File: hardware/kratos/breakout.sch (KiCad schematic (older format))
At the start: 3 parts, among them J4 Power Headers, J5 Power terminals, J6 IO Headers

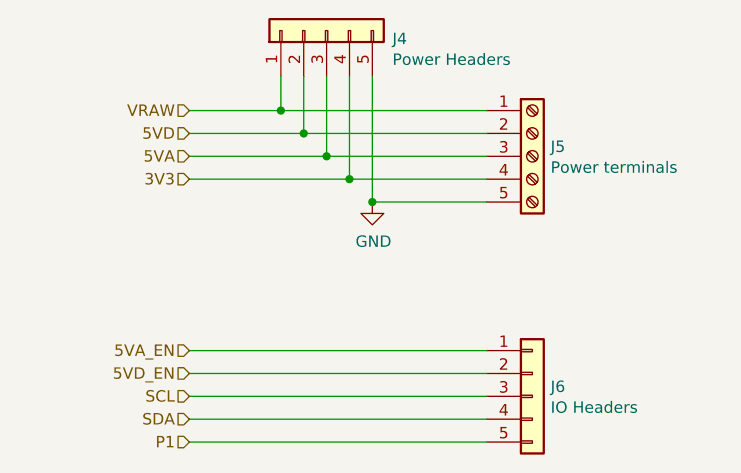
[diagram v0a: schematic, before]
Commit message: Update to linear regulators. Added PCB layout
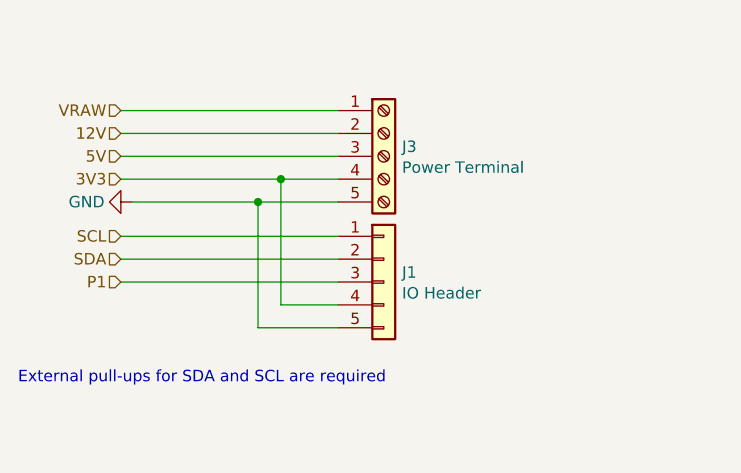
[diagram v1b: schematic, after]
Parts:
- removed J4: Power Headers, Connector_PinSocket_2.54mm:PinSocket_1x05_P2.54mm_Vertical, symbol Connector_Generic:Conn_01x05
- removed J5: Power terminals, TerminalBlock:TerminalBlock_bornier-5_P5.08mm, symbol Connector:Screw_Terminal_01x05
- removed J6: IO Headers, Connector_PinSocket_2.54mm:PinSocket_1x05_P2.54mm_Vertical, symbol Connector_Generic:Conn_01x05
- added J1: IO Header, Connector_PinSocket_2.54mm:PinSocket_1x05_P2.54mm_Vertical, symbol Connector_Generic:Conn_01x05
- added J3: Power Terminal, TerminalBlock:TerminalBlock_bornier-5_P5.08mm, symbol Connector:Screw_Terminal_01x05
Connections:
- net 3V3: now also J1.4 (Pin_4), J3.4 (Pin_4)
- net GND: now also J1.5 (Pin_5), J3.5 (Pin_5)
- net P1: now also J1.3 (Pin_3)
- net SCL: now also J1.1 (Pin_1)
- net SDA: now also J1.2 (Pin_2)
- net VRAW: now also J3.1 (Pin_1)
- new net 12V: J3.2 (Pin_2)
- new net 5V: J3.3 (Pin_3)
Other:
- note added: "External pull-ups for SDA and SCL are required\n"
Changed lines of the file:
@@
 $Descr A4 11693 8268
 encoding utf-8
-Sheet 6 6
+Sheet 3 6
 Title "Power and IO Breakout"
 Date "2021-03-06"
-Rev "REVA"
+Rev "A"
 Comp ""
 Comment1 "Author: Natesh Narain"
@@
 Comment4 ""
 $EndDescr
-Text HLabel 5450 3250 0    50   Input ~ 0
+Text HLabel 5150 3250 0    50   Input ~ 0
 VRAW
-Text HLabel 5450 3350 0    50   Input ~ 0
-5VD
-Text HLabel 5450 3450 0    50   Input ~ 0
-5VA
-Text HLabel 5450 4400 0    50   Input ~ 0
-5VD_EN
-Text HLabel 5450 4300 0    50   Input ~ 0
-5VA_EN
-Text HLabel 5450 3550 0    50   Input ~ 0
+Text HLabel 5150 3450 0    50   Input ~ 0
+5V
+Text HLabel 5150 3550 0    50   Input ~ 0
 3V3
-Text HLabel 5450 4500 0    50   Input ~ 0
+Text HLabel 5150 3800 0    50   Input ~ 0
 SCL
-Text HLabel 5450 4600 0    50   Input ~ 0
+Text HLabel 5150 3900 0    50   Input ~ 0
 SDA
-Text HLabel 5450 4700 0    50   Input ~ 0
+Text HLabel 5150 4000 0    50   Input ~ 0
 P1
 $Comp
-L Connector_Generic:Conn_01x05 J4
-U 1 1 6044FECF
-P 6050 2900
-F 0 "J4" V 6014 2612 50  0000 R CNN
-F 1 "Power Headers" V 5923 2612 50  0000 R CNN
-F 2 "Connector_PinSocket_2.54mm:PinSocket_1x05_P2.54mm_Vertical" H 6050 2900 50  0001 C CNN
-F 3 "~" H 6050 2900 50  0001 C CNN
-	1    6050 2900
-	0    -1   -1   0
+L power:GND #PWR010
+U 1 1 60452371
+P 5200 3650
+F 0 "#PWR010" H 5200 3400 50  0001 C CNN
+F 1 "GND" V 5200 3450 50  0000 C CNN
+F 2 "" H 5200 3650 50  0001 C CNN
+F 3 "" H 5200 3650 50  0001 C CNN
+	1    5200 3650
+	0    1    1    0
 $EndComp
+Text HLabel 5150 3350 0    50   Input ~ 0
+12V
 $Comp
-L Connector:Screw_Terminal_01x05 J5
-U 1 1 60450B14
-P 6950 3450
-F 0 "J5" H 7030 3492 50  0000 L CNN
-F 1 "Power terminals" H 7030 3401 50  0000 L CNN
-F 2 "TerminalBlock:TerminalBlock_bornier-5_P5.08mm" H 6950 3450 50  0001 C CNN
-F 3 "~" H 6950 3450 50  0001 C CNN
-	1    6950 3450
+L Connector:Screw_Terminal_01x05 J3
+U 1 1 604FA9FC
+P 6300 3450
+F 0 "J3" H 6380 3492 50  0000 L CNN
+F 1 "Power Terminal" H 6380 3401 50  0000 L CNN
+F 2 "TerminalBlock:TerminalBlock_bornier-5_P5.08mm" H 6300 3450 50  0001 C CNN
+F 3 "~" H 6300 3450 50  0001 C CNN
+	1    6300 3450
+	1    0    0    -1
+$EndComp
+Text Notes 4700 4450 0    50   ~ 0
+External pull-ups for SDA and SCL are required\n
+Wire Wire Line
+	5150 3250 6100 3250
+Wire Wire Line
+	5150 3350 6100 3350
+Wire Wire Line
+	5150 3450 6100 3450
+Wire Wire Line
+	5200 3650 5750 3650
+$Comp
+L Connector_Generic:Conn_01x05 J1
+U 1 1 60500B75
+P 6300 4000
+F 0 "J1" H 6380 4042 50  0000 L CNN
+F 1 "IO Header" H 6380 3951 50  0000 L CNN
+F 2 "Connector_PinSocket_2.54mm:PinSocket_1x05_P2.54mm_Vertical" H 6300 4000 50  0001 C CNN
+F 3 "~" H 6300 4000 50  0001 C CNN
+	1    6300 4000
 	1    0    0    -1
 $EndComp
 Wire Wire Line
-	5450 3250 5850 3250
+	5150 3800 6100 3800
 Wire Wire Line
-	5450 3350 5950 3350
+	5150 3900 6100 3900
 Wire Wire Line
-	5450 3450 6050 3450
+	5150 4000 6100 4000
 Wire Wire Line
-	5450 3550 6150 3550
-$Comp
-L power:GND #PWR027
-U 1 1 60452371
-P 6250 3650
-F 0 "#PWR027" H 6250 3400 50  0001 C CNN
-F 1 "GND" H 6255 3477 50  0000 C CNN
-F 2 "" H 6250 3650 50  0001 C CNN
-F 3 "" H 6250 3650 50  0001 C CNN
-	1    6250 3650
-	1    0    0    -1
-$EndComp
+	6100 4100 5850 4100
 Wire Wire Line
-	5850 3100 5850 3250
-Connection ~ 5850 3250
+	5850 4100 5850 3550
+Connection ~ 5850 3550
 Wire Wire Line
-	5850 3250 6750 3250
+	5850 3550 6100 3550
 Wire Wire Line
-	5950 3100 5950 3350
-Connection ~ 5950 3350
+	5150 3550 5850 3550
 Wire Wire Line
-	5950 3350 6750 3350
+	6100 4200 5750 4200
 Wire Wire Line
-	6050 3100 6050 3450
-Connection ~ 6050 3450
+	5750 4200 5750 3650
+Connection ~ 5750 3650
 Wire Wire Line
-	6050 3450 6750 3450
-Wire Wire Line
-	6150 3100 6150 3550
-Connection ~ 6150 3550
-Wire Wire Line
-	6150 3550 6750 3550
-Wire Wire Line
-	6250 3100 6250 3650
-Wire Wire Line
-	6750 3650 6250 3650
-Connection ~ 6250 3650
-$Comp
-L Connector_Generic:Conn_01x05 J6
-U 1 1 604539DB
-P 6950 4500
-F 0 "J6" H 7030 4542 50  0000 L CNN
-F 1 "IO Headers" H 7030 4451 50  0000 L CNN
-F 2 "Connector_PinSocket_2.54mm:PinSocket_1x05_P2.54mm_Vertical" H 6950 4500 50  0001 C CNN
-F 3 "~" H 6950 4500 50  0001 C CNN
-	1    6950 4500
-	1    0    0    -1
-$EndComp
-Wire Wire Line
-	5450 4300 6750 4300
-Wire Wire Line
-	5450 4400 6750 4400
-Wire Wire Line
-	5450 4500 6750 4500
-Wire Wire Line
-	5450 4600 6750 4600
-Wire Wire Line
-	5450 4700 6750 4700
+	5750 3650 6100 3650
 $EndSCHEMATC

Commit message: Rev B
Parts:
- removed J3: Power Terminal, TerminalBlock:TerminalBlock_bornier-5_P5.08mm, symbol Connector:Screw_Terminal_01x05
- added J3: Power Terminal, Connector_PinHeader_2.54mm:PinHeader_1x05_P2.54mm_Vertical, symbol Connector_Generic:Conn_01x05
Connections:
- net 3V3: now also J3.4 (Pin_4)
- net 5V: now also J3.2 (Pin_2)
- net GND: now also J3.5 (Pin_5)
- net VRAW: now also J3.1 (Pin_1)
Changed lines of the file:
@@
 $Descr A4 11693 8268
 encoding utf-8
-Sheet 3 6
+Sheet 3 5
 Title "Power and IO Breakout"
 Date "2021-03-06"
@@
 Text HLabel 5150 3250 0    50   Input ~ 0
 VRAW
-Text HLabel 5150 3450 0    50   Input ~ 0
+Text HLabel 5150 3350 0    50   Input ~ 0
 5V
 Text HLabel 5150 3550 0    50   Input ~ 0
@@
 	0    1    1    0
 $EndComp
-Text HLabel 5150 3350 0    50   Input ~ 0
-12V
-$Comp
-L Connector:Screw_Terminal_01x05 J3
-U 1 1 604FA9FC
-P 6300 3450
-F 0 "J3" H 6380 3492 50  0000 L CNN
-F 1 "Power Terminal" H 6380 3401 50  0000 L CNN
-F 2 "TerminalBlock:TerminalBlock_bornier-5_P5.08mm" H 6300 3450 50  0001 C CNN
-F 3 "~" H 6300 3450 50  0001 C CNN
-	1    6300 3450
-	1    0    0    -1
-$EndComp
 Text Notes 4700 4450 0    50   ~ 0
 External pull-ups for SDA and SCL are required\n
 Wire Wire Line
 	5150 3250 6100 3250
-Wire Wire Line
-	5150 3350 6100 3350
-Wire Wire Line
-	5150 3450 6100 3450
 Wire Wire Line
 	5200 3650 5750 3650
@@
 Wire Wire Line
 	5750 3650 6100 3650
+$Comp
+L Connector_Generic:Conn_01x05 J3
+U 1 1 60AC5538
+P 6300 3450
+F 0 "J3" H 6380 3492 50  0000 L CNN
+F 1 "Power Terminal" H 6380 3401 50  0000 L CNN
+F 2 "Connector_PinHeader_2.54mm:PinHeader_1x05_P2.54mm_Vertical" H 6300 3450 50  0001 C CNN
+F 3 "~" H 6300 3450 50  0001 C CNN
+	1    6300 3450
+	1    0    0    -1
+$EndComp
+Wire Wire Line
+	5150 3350 6100 3350
 $EndSCHEMATC
